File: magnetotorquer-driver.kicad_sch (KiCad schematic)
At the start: 59 parts, among them U10 MAX7311AAG+, U11 MCP47FVB24-E/MQ, U12 ALM2402QPWPRQ1, U13 OPA340MDBVTEP, U14 AD7091R-5BCPZ-RL7, U15 ALM2402QPWPRQ1

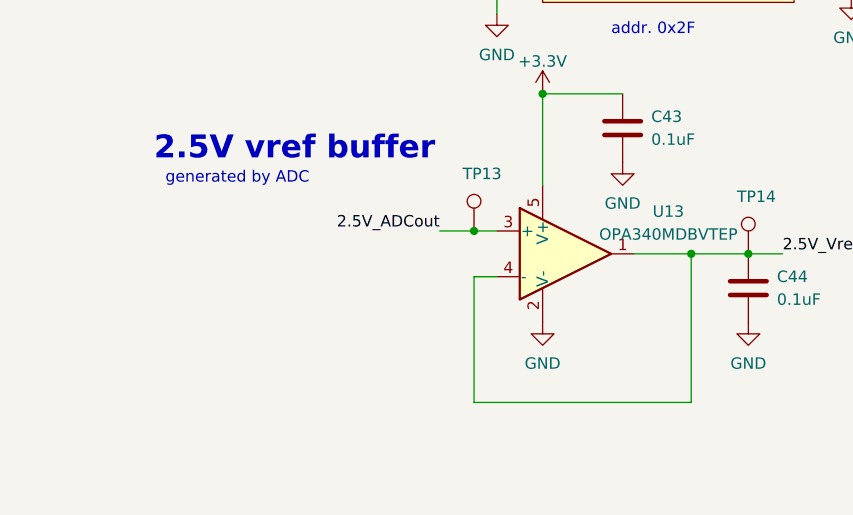
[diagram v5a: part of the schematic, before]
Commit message: added current sensors and other design changes
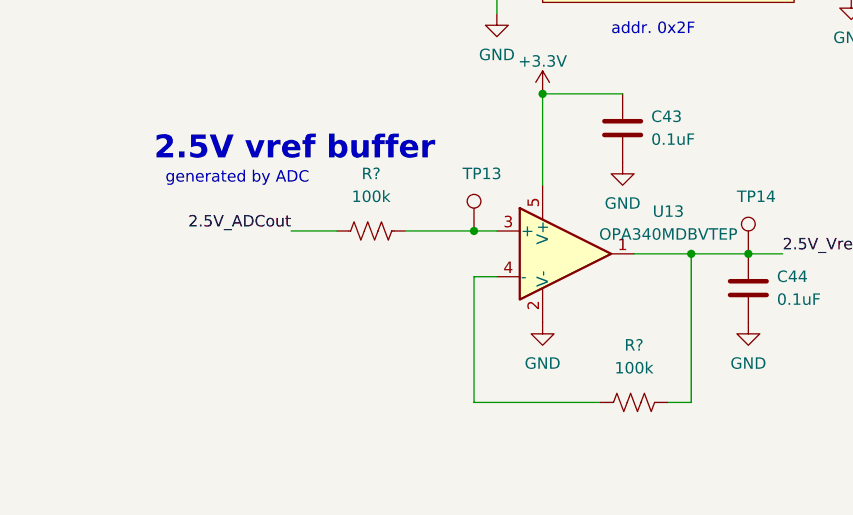
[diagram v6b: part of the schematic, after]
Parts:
- added R? (x2): 100k, symbol Device:R_US
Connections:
- net 2.5V_ADCout: now also R?.1; no longer TP13.1, U13.3 (+)
- net 2.5V_Vref: now also R?.2; no longer U13.4 (-)
- new net: R?.2, TP13.1, U13.3 (+)
- new net: R?.1, U13.4 (-)
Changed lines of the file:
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@@
   (no_connect (at 344.17 151.13))
   (no_connect (at 92.71 49.53))
+  (wire (pts (xy 360.68 219.71) (xy 363.22 219.71))
+    (stroke (width 0) (type default) (color 0 0 0 0))
+  )
   (wire (pts (xy 45.72 41.91) (xy 45.72 43.18))
     (stroke (width 0) (type default) (color 0 0 0 0))
@@
     (stroke (width 0) (type default) (color 0 0 0 0))
   )
-  (wire (pts (xy 339.09 219.71) (xy 363.22 219.71))
+  (wire (pts (xy 339.09 219.71) (xy 353.06 219.71))
     (stroke (width 0) (type default) (color 0 0 0 0))
   )
@@
     (stroke (width 0) (type default) (color 0 0 0 0))
   )
+  (wire (pts (xy 318.77 200.66) (xy 323.85 200.66))
+    (stroke (width 0) (type default) (color 0 0 0 0))
+  )
   (wire (pts (xy 341.63 168.91) (xy 344.17 168.91))
     (stroke (width 0) (type default) (color 0 0 0 0))
@@
     (stroke (width 0) (type default) (color 0 0 0 0))
   )
-  (wire (pts (xy 335.28 200.66) (xy 339.09 200.66))
-    (stroke (width 0) (type default) (color 0 0 0 0))
-  )
   (wire (pts (xy 36.83 41.91) (xy 45.72 41.91))
     (stroke (width 0) (type default) (color 0 0 0 0))
@@
     (stroke (width 0) (type default) (color 0 0 0 0))
   )
+  (wire (pts (xy 331.47 200.66) (xy 339.09 200.66))
+    (stroke (width 0) (type default) (color 0 0 0 0))
+  )
   (wire (pts (xy 69.85 66.04) (xy 72.39 66.04))
     (stroke (width 0) (type default) (color 0 0 0 0))
@@
     (effects (font (size 1.27 1.27)) (justify right bottom))
   )
-  (label "2.5V_ADCout" (at 335.28 200.66 180)
+  (label "2.5V_ADCout" (at 318.77 200.66 180)
     (effects (font (size 1.27 1.27)) (justify right bottom))
   )
@@
     (pin "1")
   )
+  (symbol (lib_id "Device:R_US") (at 327.66 200.66 90) (unit 1)
+    (in_bom yes) (on_board yes) (fields_autoplaced)
+    (property "Reference" "R?" (id 0) (at 327.66 194.31 90))
+    (property "Value" "100k" (id 1) (at 327.66 196.85 90))
+    (property "Footprint" "" (id 2) (at 327.914 199.644 90)
+      (effects (font (size 1.27 1.27)) hide)
+    )
+    (property "Datasheet" "~" (id 3) (at 327.66 200.66 0)
+      (effects (font (size 1.27 1.27)) hide)
+    )
+    (pin "1")
+    (pin "2")
+  )
   (symbol (lib_id "Device:R_US") (at 66.04 68.58 90) (unit 1)
     (in_bom yes) (on_board yes)
@@
       (effects (font (size 1.27 1.27)) hide)
     )
+    (pin "1")
+    (pin "2")
+  )
+  (symbol (lib_id "Device:R_US") (at 356.87 219.71 90) (unit 1)
+    (in_bom yes) (on_board yes) (fields_autoplaced)
+    (property "Reference" "R?" (id 0) (at 356.87 213.36 90))
+    (property "Value" "100k" (id 1) (at 356.87 215.9 90))
+    (property "Footprint" "" (id 2) (at 357.124 218.694 90)
+      (effects (font (size 1.27 1.27)) hide)
+    )
+    (property "Datasheet" "~" (id 3) (at 356.87 219.71 0)
+      (effects (font (size 1.27 1.27)) hide)
+    )

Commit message: finished routing
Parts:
- R93: renamed from R?; footprint (none) -> Resistor_SMD:R_0603_1608Metric
- gave numbers to parts that had none: 1
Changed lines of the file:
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@@
   (symbol (lib_id "Device:R_US") (at 327.66 200.66 90) (unit 1)
     (in_bom yes) (on_board yes) (fields_autoplaced)
-    (property "Reference" "R?" (id 0) (at 327.66 194.31 90))
+    (property "Reference" "R93" (id 0) (at 327.66 194.31 90))
     (property "Value" "100k" (id 1) (at 327.66 196.85 90))
-    (property "Footprint" "" (id 2) (at 327.914 199.644 90)
+    (property "Footprint" "Resistor_SMD:R_0603_1608Metric" (id 2) (at 327.914 199.644 90)
       (effects (font (size 1.27 1.27)) hide)
     )
@@
   (symbol (lib_id "Device:R_US") (at 356.87 219.71 90) (unit 1)
     (in_bom yes) (on_board yes) (fields_autoplaced)
-    (property "Reference" "R?" (id 0) (at 356.87 213.36 90))
+    (property "Reference" "R102" (id 0) (at 356.87 213.36 90))
     (property "Value" "100k" (id 1) (at 356.87 215.9 90))
     (property "Footprint" "" (id 2) (at 357.124 218.694 90)

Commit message: misc
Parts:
- added R?: 100k, Resistor_SMD:R_0603_1608Metric, symbol Device:R_US
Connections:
- net +3V3: now also R?.2
- net +5V: no longer R35.1, R42.1
- net GND: now also R35.1, R42.1
- net ~{ADC_RST}: now also R?.1
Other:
- note removed: "check for pulldowns on DAC lines"
- moved on the sheet: C32, C33, C38, C41, R35, R39, R40, R41, R42
